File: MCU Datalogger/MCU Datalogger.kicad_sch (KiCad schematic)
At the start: 0 parts

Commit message: main: setup of EE schema for new project
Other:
- company: (none) -> Heratek
- title: (none) -> ${project_name}
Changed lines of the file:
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@@
 	(generator_version "9.0")
 	(paper "A4")
+	(title_block
+		(title "${project_name}")
+		(date "2026-03-08")
+		(rev "1")
+		(company "Heratek")
+		(comment 1 "Designed by Bankole Olonilua")
+	)
 	(sheet_instances
 		(path "/"

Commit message: main: Added symbols to schematic sheets
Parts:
- added BT1: Battery, symbol Device:Battery
- added C1, C2, C3, C4: C, symbol Device:C
- added C5, C6: C_Polarized, symbol Device:C_Polarized
- added D1, D2: LED, symbol Device:LED
- added H1, H2, H3, H4: MountingHole, symbol Mechanical:MountingHole
- added R1, R2, R3, R4, R5, R6, R7: R_US, symbol Device:R_US
- added U1, U2: 24LC1025, symbol Memory_EEPROM:24LC1025
- added U3: DS1337S_, DS1337S_:SOIC127P600X175-8N, symbol DS1337S_:DS1337S_
- added U4: ATMEGA328P-AU, ATMEGA328P-AU:QFP80P900X900X120-32N, symbol ATMEGA328P-AU:ATMEGA328P-AU
- added Y1, Y2: Crystal, symbol Device:Crystal
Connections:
- new net GND: U4.21 (GND), U4.3 (GND), U4.5 (GND)
- new net VCC: U4.4 (VCC), U4.6 (VCC)
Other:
- added sheet Connectors (Connectors.kicad_sch)

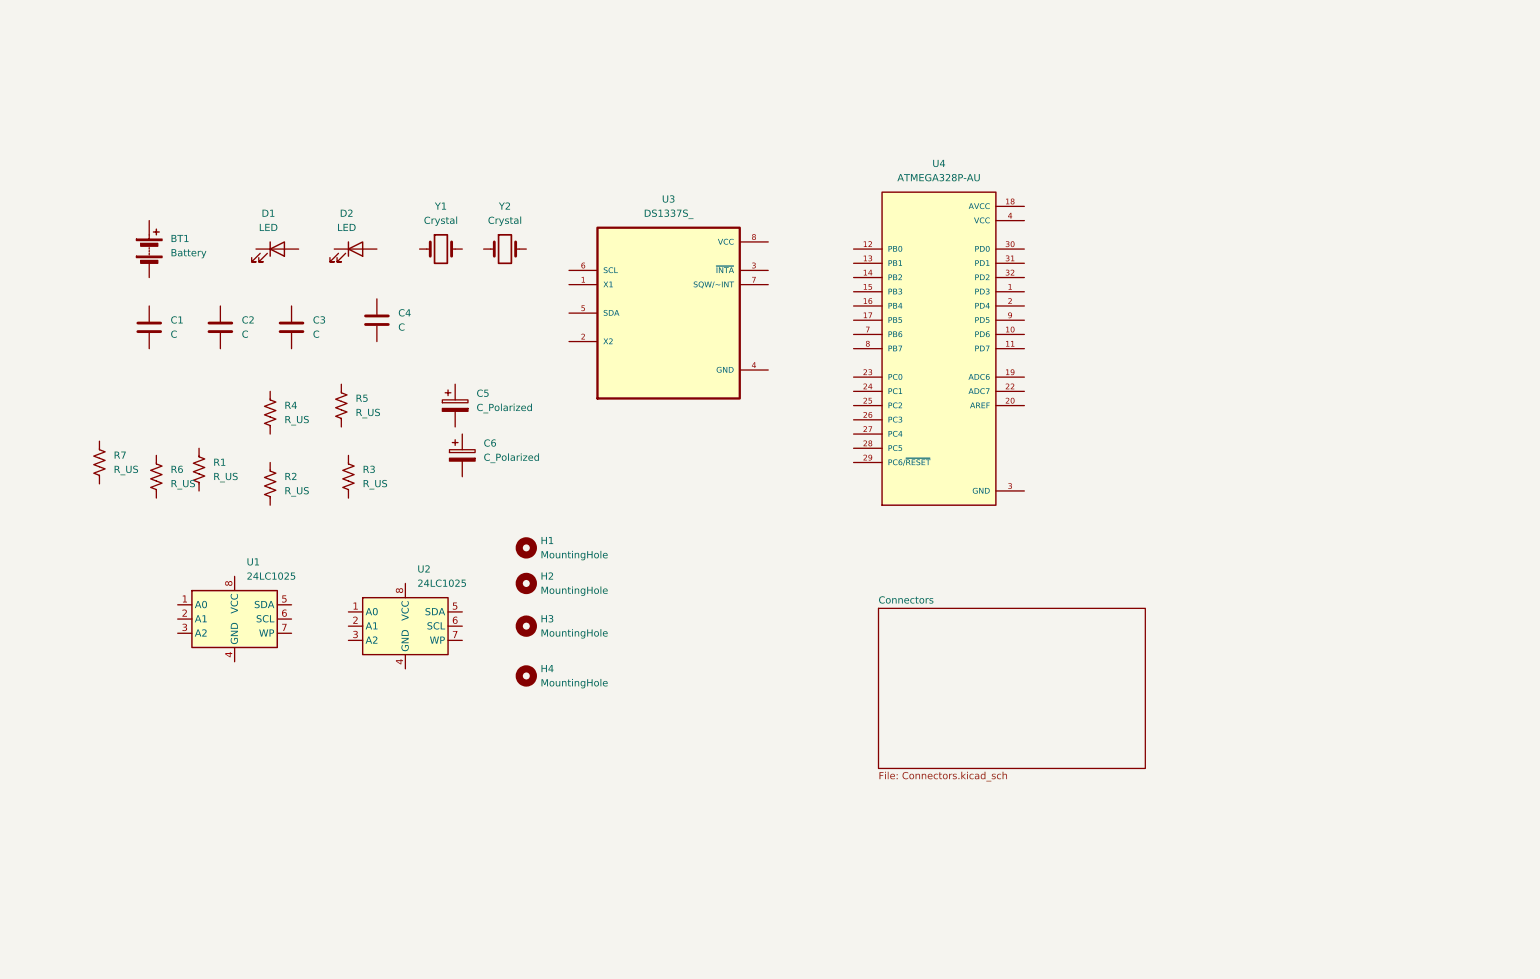
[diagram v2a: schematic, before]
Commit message: main: Annotated symbol in schematic as needed
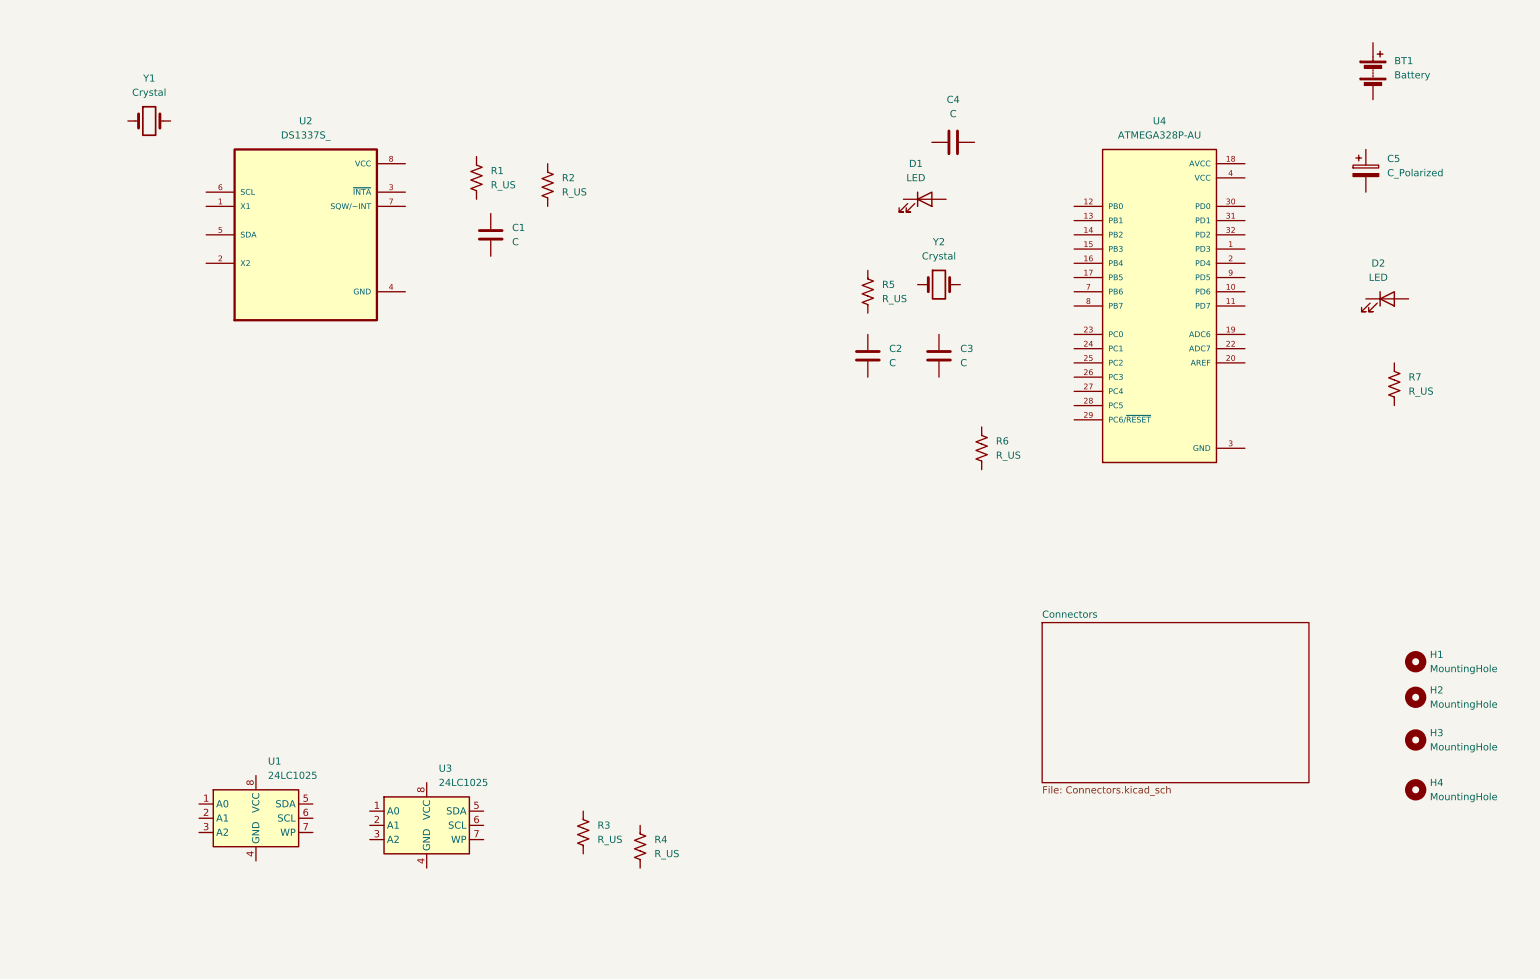
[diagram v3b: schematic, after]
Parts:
- removed C6: C_Polarized, symbol Device:C_Polarized
- renumbered C4 to C1, C1 to C4, R3 to R1, R7 to R3, R6 to R4, R4 to R5, R1 to R6, R5 to R7, U3 to U2, U2 to U3
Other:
- moved on the sheet: BT1, C1, C2, C3, C4, C5, D1, D2, H1, H2, H3, H4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

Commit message: main: Added component values
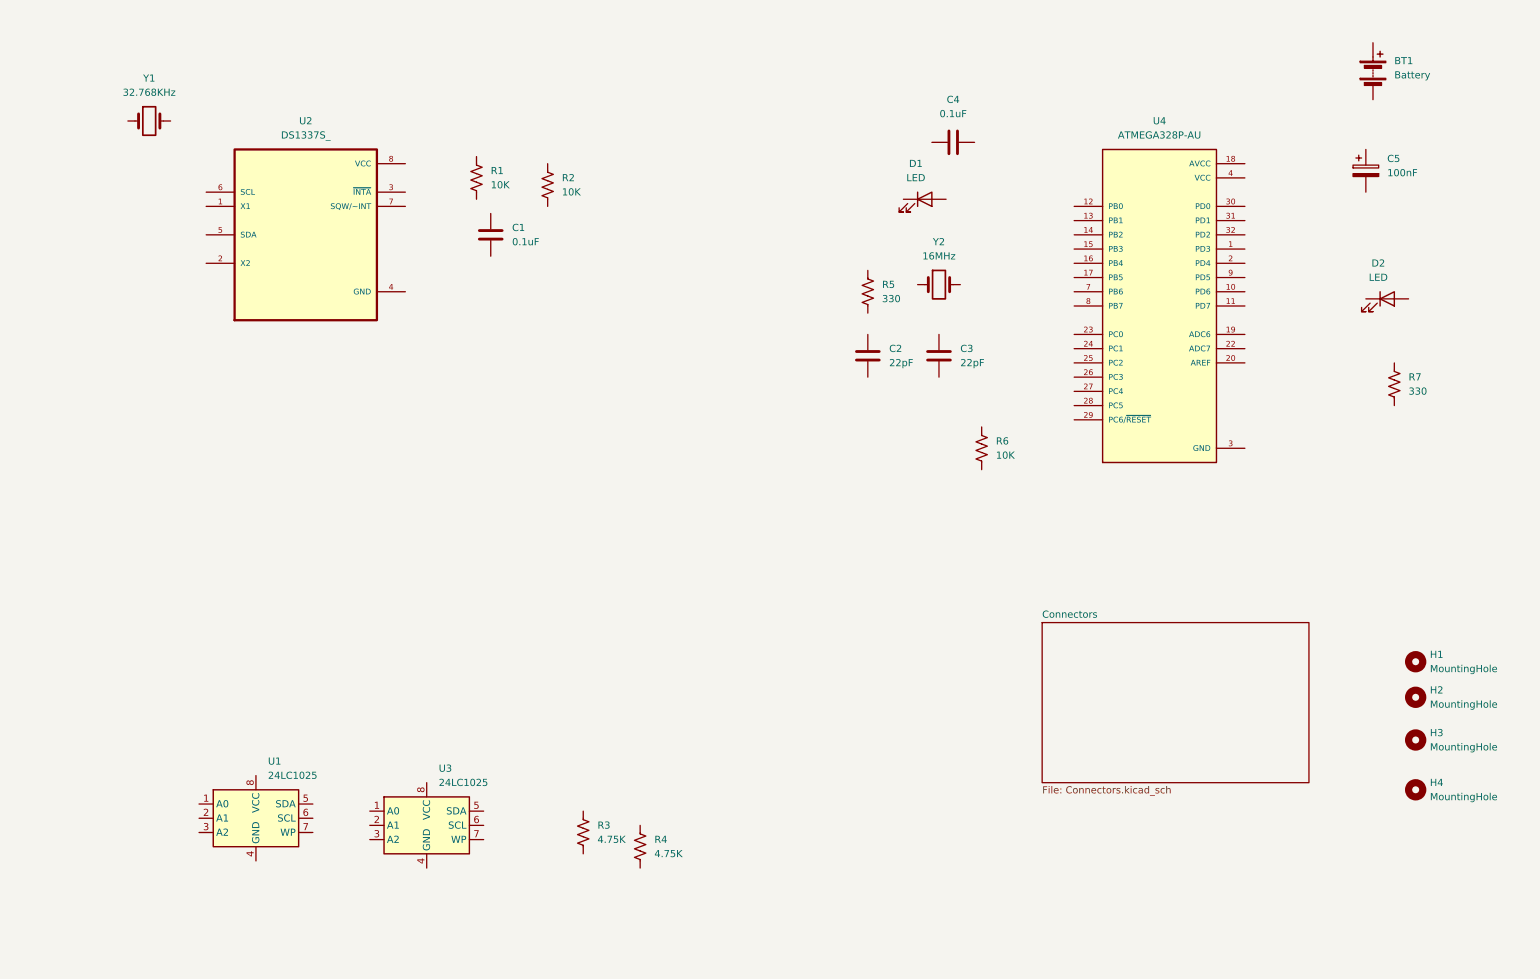
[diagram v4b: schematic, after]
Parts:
- C1, C4: value C -> 0.1uF
- C2, C3: value C -> 22pF
- C5: value C_Polarized -> 100nF
- R1, R2, R6: value R_US -> 10K
- R3, R4: value R_US -> 4.75K
- R5, R7: value R_US -> 330
- Y1: value Crystal -> 32.768KHz
- Y2: value Crystal -> 16MHz
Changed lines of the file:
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@@
 			)
 		)
-		(property "Value" "C_Polarized"
+		(property "Value" "100nF"
 			(at 257.81 46.1009 0)
 			(effects
@@
 			)
 		)
+		(property "Purpose" ""
+			(at 254 45.72 0)
+			(effects
+				(font
+					(size 1.27 1.27)
+				)
+				(hide yes)
+			)
+		)
 		(pin "1"
 		)
@@
 			)
 		)
-		(property "Value" "Crystal"
+		(property "Value" "32.768KHz"
 			(at 36.83 31.75 0)
 			(effects
@@
 			)
 		)
+		(property "Purpose" ""
+			(at 36.83 36.83 0)
+			(effects
+				(font
+					(size 1.27 1.27)
+				)
+				(hide yes)
+			)
+		)
 		(pin "2"
 		)
@@
 			)
 		)
-		(property "Value" "C"
+		(property "Value" "0.1uF"
 			(at 101.6 58.4199 0)
 			(effects
@@
 			)
 		)
+		(property "Purpose" ""
+			(at 97.79 57.15 0)
+			(effects
+				(font
+					(size 1.27 1.27)
+				)
+				(hide yes)
+			)
+		)
 		(pin "1"
 		)
@@
 			)
 		)
-		(property "Value" "C"
+		(property "Value" "0.1uF"
 			(at 180.34 35.56 90)
 			(effects
@@
 			)
 		)
+		(property "Purpose" ""
+			(at 180.34 40.64 0)
+			(effects
+				(font
+					(size 1.27 1.27)
+				)
+				(hide yes)
+			)
+		)
 		(pin "1"
 		)
@@
 			)
 		)
-		(property "Value" "R_US"
+		(property "Value" "10K"
 			(at 110.49 49.5299 0)
 			(effects
@@
 			)
 		)
+		(property "Purpose" ""
+			(at 107.95 48.26 0)
+			(effects
+				(font
+					(size 1.27 1.27)
+				)
+				(hide yes)
+			)
+		)
 		(pin "2"
 		)
@@
 			)
 		)
-		(property "Value" "Crystal"
+		(property "Value" "16MHz"
 			(at 177.8 60.96 0)
 			(effects
@@
 			)
 		)
+		(property "Purpose" ""
+			(at 177.8 66.04 0)
+			(effects
+				(font
+					(size 1.27 1.27)
+				)
+				(hide yes)
+			)
+		)
 		(pin "2"
 		)
@@
 			)
 		)
-		(property "Value" "R_US"
+		(property "Value" "330"
 			(at 167.64 68.5799 0)
 			(effects
@@
 			)
 		)
+		(property "Purpose" ""
+			(at 165.1 67.31 0)
+			(effects
+				(font
+					(size 1.27 1.27)
+				)
+				(hide yes)
+			)
+		)
 		(pin "2"
 		)
@@
 			)
 		)
-		(property "Value" "R_US"
+		(property "Value" "4.75K"
 			(at 116.84 165.0999 0)
 			(effects
@@
 			)
 		)
+		(property "Purpose" ""
+			(at 114.3 163.83 0)
+			(effects
+				(font
+					(size 1.27 1.27)
+				)
+				(hide yes)
+			)
+		)
 		(pin "2"
 		)
@@
 			)
 		)
-		(property "Value" "R_US"
+		(property "Value" "10K"
 			(at 97.79 48.2599 0)
 			(effects
@@
 			)
 		)
+		(property "Purpose" ""
+			(at 95.25 46.99 0)
+			(effects
+				(font
+					(size 1.27 1.27)
+				)
+				(hide yes)
+			)
+		)
 		(pin "2"
 		)
@@
 			)
 		)
-		(property "Value" "R_US"
+		(property "Value" "4.75K"
 			(at 127 167.6399 0)
 			(effects
@@
 			)
 		)
+		(property "Purpose" ""
+			(at 124.46 166.37 0)
+			(effects
+				(font
+					(size 1.27 1.27)
+				)
+				(hide yes)
+			)
+		)
 		(pin "2"
 		)
@@
 			)
 		)
-		(property "Value" "R_US"
+		(property "Value" "10K"
 			(at 187.96 96.5199 0)
 			(effects
@@
 			)
 		)
+		(property "Purpose" ""
+			(at 185.42 95.25 0)
+			(effects
+				(font
+					(size 1.27 1.27)
+				)
+				(hide yes)
+			)
+		)
 		(pin "2"
 		)
@@
 			)
 		)
-		(property "Value" "C"
+		(property "Value" "22pF"
 			(at 168.91 80.0099 0)
 			(effects
@@
 			)
 		)
+		(property "Purpose" ""
+			(at 165.1 78.74 0)
+			(effects
+				(font
+					(size 1.27 1.27)
+				)
+				(hide yes)
+			)
+		)
 		(pin "1"
 		)
@@
 			)
 		)
-		(property "Value" "R_US"
+		(property "Value" "330"
 			(at 261.62 85.0899 0)
 			(effects
@@
 			)
 		)
+		(property "Purpose" ""
+			(at 259.08 83.82 0)
+			(effects
+				(font
+					(size 1.27 1.27)
+				)
+				(hide yes)
+			)
+		)
 		(pin "2"
 		)
@@
 			)
 		)
-		(property "Value" "C"
+		(property "Value" "22pF"
 			(at 181.61 80.0099 0)
 			(effects
@@
 			(at 177.8 78.74 0)
 			(effects
+				(font
+					(size 1.27 1.27)
+				)
+				(hide yes)
+			)
+		)
+		(property "Purpose" ""
+			(at 177.8 78.74 0)
+			(effects

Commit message: main: Assigned footprints to all parts
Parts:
- BT1: footprint (none) -> Connector_PinHeader_2.54mm:PinHeader_1x02_P2.54mm_Vertical
- C1, C2, C3, C4, C5: footprint (none) -> Capacitor_SMD:C_0805_2012Metric
- D1, D2: footprint (none) -> LED_SMD:LED_0805_2012Metric
- H1, H2, H3, H4: footprint (none) -> MountingHole:MountingHole_2.1mm
- R1, R2, R3, R4, R5, R6, R7: footprint (none) -> Resistor_SMD:R_0805_2012Metric
- U1, U3: footprint (none) -> Package_SO:SOIC-8_5.3x5.3mm_P1.27mm
- Y1, Y2: footprint (none) -> Crystal:Crystal_SMD_5032-2Pin_5.0x3.2mm_HandSoldering
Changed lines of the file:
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@@
 			)
 		)
-		(property "Footprint" ""
+		(property "Footprint" "Capacitor_SMD:C_0805_2012Metric"
 			(at 254.9652 49.53 0)
 			(effects
@@
 			)
 		)
-		(property "Footprint" ""
+		(property "Footprint" "MountingHole:MountingHole_2.1mm"
 			(at 262.89 147.32 0)
 			(effects
@@
 			)
 		)
-		(property "Footprint" ""
+		(property "Footprint" "LED_SMD:LED_0805_2012Metric"
 			(at 175.26 50.8 0)
 			(effects
@@
 			)
 		)
-		(property "Footprint" ""
+		(property "Footprint" "Crystal:Crystal_SMD_5032-2Pin_5.0x3.2mm_HandSoldering"
 			(at 36.83 36.83 0)
 			(effects
@@
 			)
 		)
-		(property "Footprint" ""
+		(property "Footprint" "MountingHole:MountingHole_2.1mm"
 			(at 262.89 133.35 0)
 			(effects
@@
 			)
 		)
-		(property "Footprint" ""
+		(property "Footprint" "Capacitor_SMD:C_0805_2012Metric"
 			(at 98.7552 60.96 0)
 			(effects
@@
 			)
 		)
-		(property "Footprint" ""
+		(property "Footprint" "Package_SO:SOIC-8_5.3x5.3mm_P1.27mm"
 			(at 55.88 161.29 0)
 			(effects
@@
 			)
 		)
-		(property "Footprint" ""
+		(property "Footprint" "Package_SO:SOIC-8_5.3x5.3mm_P1.27mm"
 			(at 86.36 162.56 0)
 			(effects
@@
 			)
 		)
-		(property "Footprint" ""
+		(property "Footprint" "Capacitor_SMD:C_0805_2012Metric"
 			(at 184.15 39.6748 0)
 			(effects
@@
 			)
 		)
-		(property "Footprint" ""
+		(property "Footprint" "Resistor_SMD:R_0805_2012Metric"
 			(at 108.966 48.514 90)
 			(effects
@@
 			)
 		)
-		(property "Footprint" ""
+		(property "Footprint" "Crystal:Crystal_SMD_5032-2Pin_5.0x3.2mm_HandSoldering"
 			(at 177.8 66.04 0)
 			(effects
@@
 			)
 		)
-		(property "Footprint" ""
+		(property "Footprint" "LED_SMD:LED_0805_2012Metric"
 			(at 257.81 68.58 0)
 			(effects
@@
 			)
 		)
-		(property "Footprint" ""
+		(property "Footprint" "Resistor_SMD:R_0805_2012Metric"
 			(at 166.116 67.564 90)
 			(effects
@@
 			)
 		)
-		(property "Footprint" ""
+		(property "Footprint" "Resistor_SMD:R_0805_2012Metric"
 			(at 115.316 164.084 90)
 			(effects
@@
 			)
 		)
-		(property "Footprint" ""
+		(property "Footprint" "MountingHole:MountingHole_2.1mm"
 			(at 262.89 139.7 0)
 			(effects
@@
 			)
 		)
-		(property "Footprint" ""
+		(property "Footprint" "Resistor_SMD:R_0805_2012Metric"
 			(at 96.266 47.244 90)
 			(effects
@@
 			)
 		)
-		(property "Footprint" ""
+		(property "Footprint" "Resistor_SMD:R_0805_2012Metric"
 			(at 125.476 166.624 90)
 			(effects
@@
 			)
 		)
-		(property "Footprint" ""
+		(property "Footprint" "Connector_PinHeader_2.54mm:PinHeader_1x02_P2.54mm_Vertical"
 			(at 255.27 26.416 90)
 			(effects
@@
 			)
 		)
-		(property "Footprint" ""
+		(property "Footprint" "Resistor_SMD:R_0805_2012Metric"
 			(at 186.436 95.504 90)
 			(effects
@@
 			)
 		)
-		(property "Footprint" ""
+		(property "Footprint" "MountingHole:MountingHole_2.1mm"
 			(at 262.89 156.21 0)
 			(effects
@@
 			)
 		)
-		(property "Footprint" ""
+		(property "Footprint" "Capacitor_SMD:C_0805_2012Metric"
 			(at 166.0652 82.55 0)
 			(effects
@@
 			)
 		)
-		(property "Footprint" ""
+		(property "Footprint" "Resistor_SMD:R_0805_2012Metric"
 			(at 260.096 84.074 90)
 			(effects
@@
 			)
 		)
-		(property "Footprint" ""
+		(property "Footprint" "Capacitor_SMD:C_0805_2012Metric"
 			(at 178.7652 82.55 0)
 			(effects
